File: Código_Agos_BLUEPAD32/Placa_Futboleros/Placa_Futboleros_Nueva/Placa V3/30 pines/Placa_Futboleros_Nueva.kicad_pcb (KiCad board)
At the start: 2 copper layers, 52 x 100 mm, 17 parts, among them J1 BAT, J2 Motor_Izq_Adelante, J3 Motor_Izq_Atras, J4 Motor_Der_Adelante, J5 Motor_Der_Atras, U1 LM7805, U3 DRV8833, U4 DRV8833, U5 ESP32-DEVKIT-V1

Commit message: Idea e Implementación Futura para Placa 30 pines V3
Se agrega un divisor resistivo de las baterías al ADC para monitoreo
y lectura del voltaje de las baterías para mnostrar en la web cuando
se active el AP; con el fin de también poseer un historial de mediciones
y calcular la cantidad de partidos.

También conviene para regular el PWM en función del voltaje
recibido para mantener la potencia en los motores.
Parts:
- added R2: 100k, Resistor_THT:R_Axial_DIN0207_L6.3mm_D2.5mm_P10.16mm_Horizontal, F.Cu at (108.2, 129.5)
- added R3: 47k, Resistor_THT:R_Axial_DIN0207_L6.3mm_D2.5mm_P10.16mm_Horizontal, F.Cu at (112.3, 129.5)
- D2: value LED -> LED_RED
- U1: value LM7805 -> LM7805_TO220
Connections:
- U5 pad 21: unconnected-(U5-D32-Pad21) -> /ADC
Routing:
- net GND: track 204.6 -> 248.3 mm
- net VCC: track 139.8 -> 175.0 mm
- net /ADC: track 0.00 -> 27.0 mm
- net IN_M1A: track 88.1 -> 93.8 mm

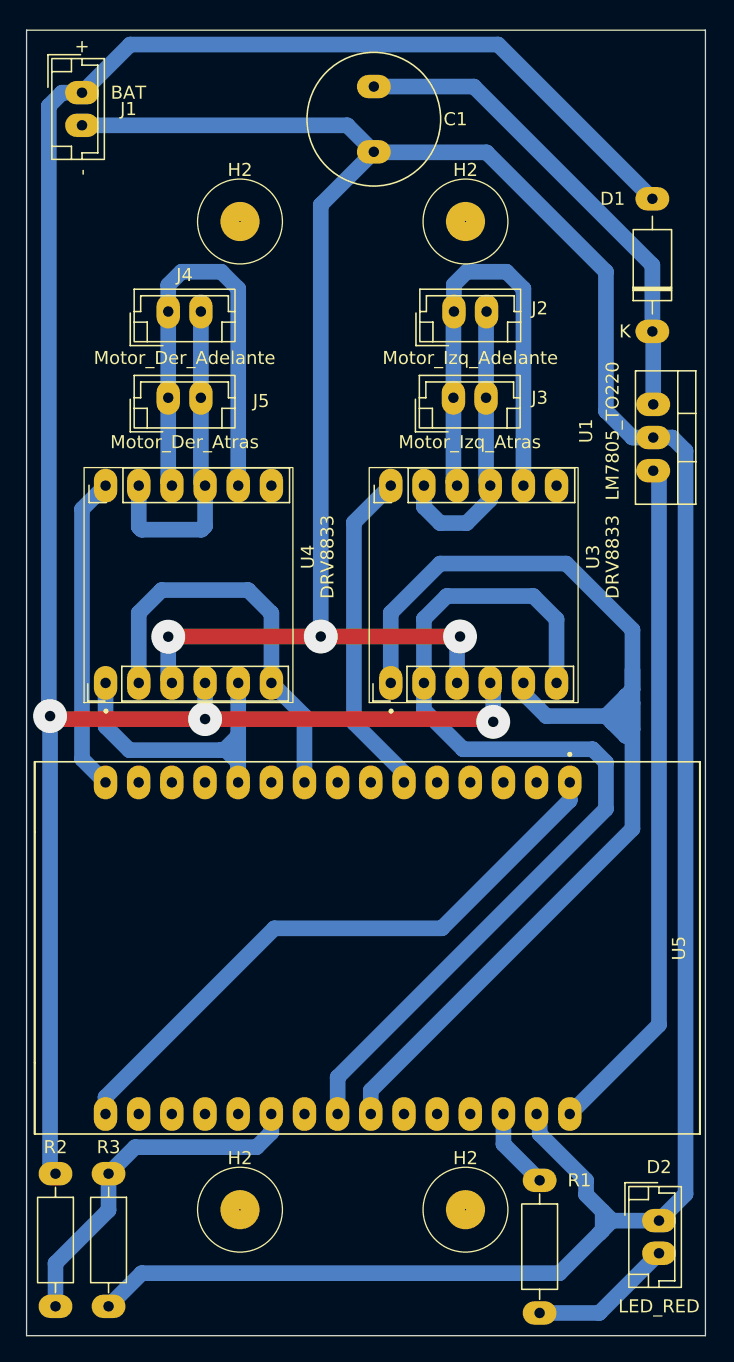
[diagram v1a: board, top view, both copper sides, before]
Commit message: Impresión en PDF de placas para planchado
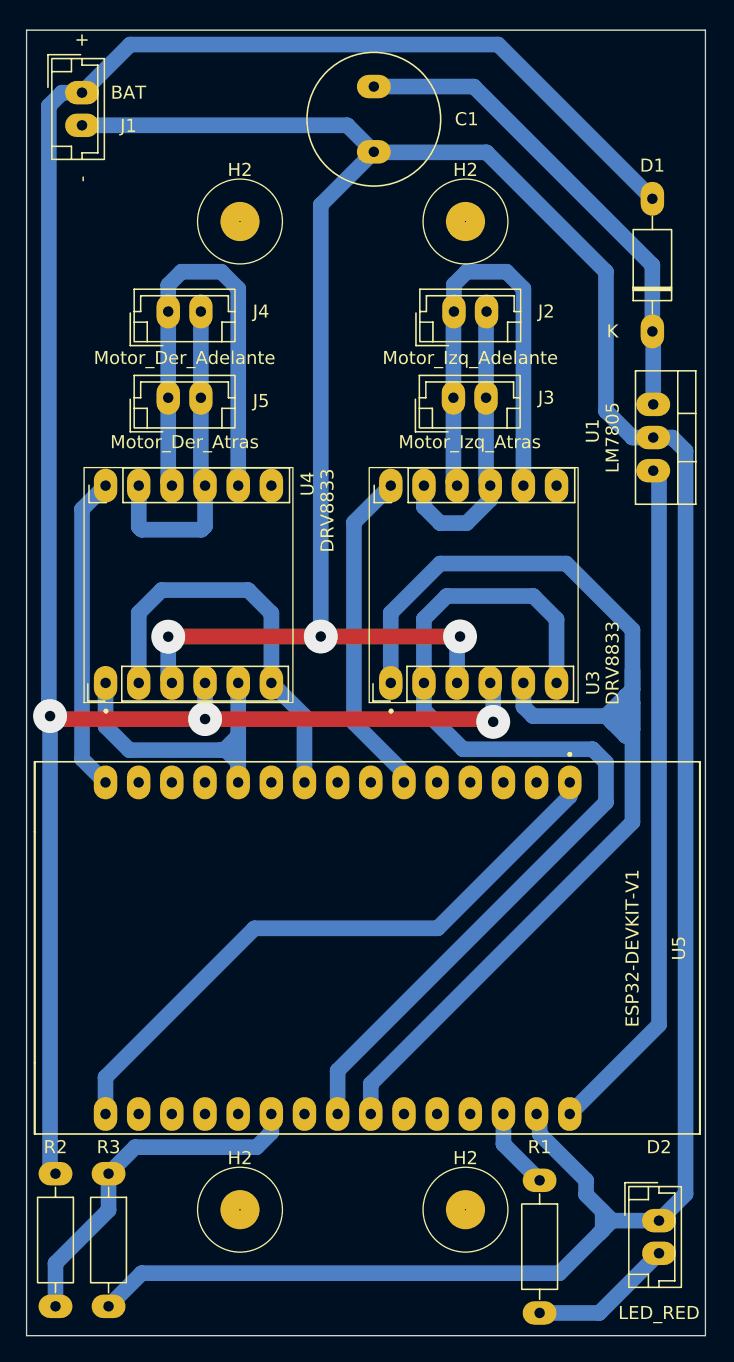
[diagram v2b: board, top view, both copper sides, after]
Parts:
- U1: value LM7805_TO220 -> LM7805
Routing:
- net GND: track 248.3 -> 524.4 mm, vias 3 -> 6
- net VCC: track 175.0 -> 0.00 mm, vias 3 -> 0
- net +5V: track 52.3 -> 0.00 mm
- net Net-(D1-K): track 37.7 -> 0.00 mm
- net Net-(J2-Pin_2): track 22.5 -> 59.4 mm
- net Net-(J2-Pin_1): track 36.9 -> 0.00 mm
- net Net-(J4-Pin_2): track 25.0 -> 61.9 mm
- net Net-(J4-Pin_1): track 36.9 -> 0.00 mm
- net Net-(D2-A): track 11.0 -> 0.00 mm
- net +3.3V: track 47.6 -> 48.3 mm
- net IN_M1A: track 93.8 -> 94.4 mm
